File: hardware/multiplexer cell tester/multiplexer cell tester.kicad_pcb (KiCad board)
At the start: 2 copper layers, 143 x 118 mm, 152 parts, among them J1 Conn_01x10_Female, J10 Panel 3, J11 Conn_01x03_Male, J12 Conn_01x03_Male, J13 Conn_01x03_Male, J14 0781710004, J15 Radio, J16 Power, J17 Conn_01x01_Male, J2 Conn_01x10_Female, J3 Conn_01x10_Female, J4 Conn_01x10_Female, J5 A2 Select, J6 A1 Select, J7 A0 Select, J8 Panel 1, J9 Panel 2, U1 SN74LVC1G14DRL, U10 ADG839YKSZ-REEL7, U11 ADG839YKSZ-REEL7, U12 ADG839YKSZ-REEL7, U13 74HC590, U14 ADG841YKSZ-500RL7, U15 ADG841YKSZ-500RL7, U16 ADG841YKSZ-500RL7, U17 ADG841YKSZ-500RL7, U18 ADG841YKSZ-500RL7, U19 ADG841YKSZ-500RL7, U2 SN74LVC1G14DRL, U20 ADG841YKSZ-500RL7, U21 ADG841YKSZ-500RL7, U22 INA190A4IDDFR, U23 OPA2387, U24 INA190A4IDDFR, U25 INA190A4IDDFR, U26 INA190A4IDDFR, U27 LT6654AMPS6-1.25, U28 LT6654AHS6-3.3, U3 CD4518BM96, U4 CD4514BM, U5 ADG839YKSZ-REEL7, U6 ADG839YKSZ-REEL7, U7 ADG839YKSZ-REEL7, U8 ADG839YKSZ-REEL7, U9 ADG839YKSZ-REEL7

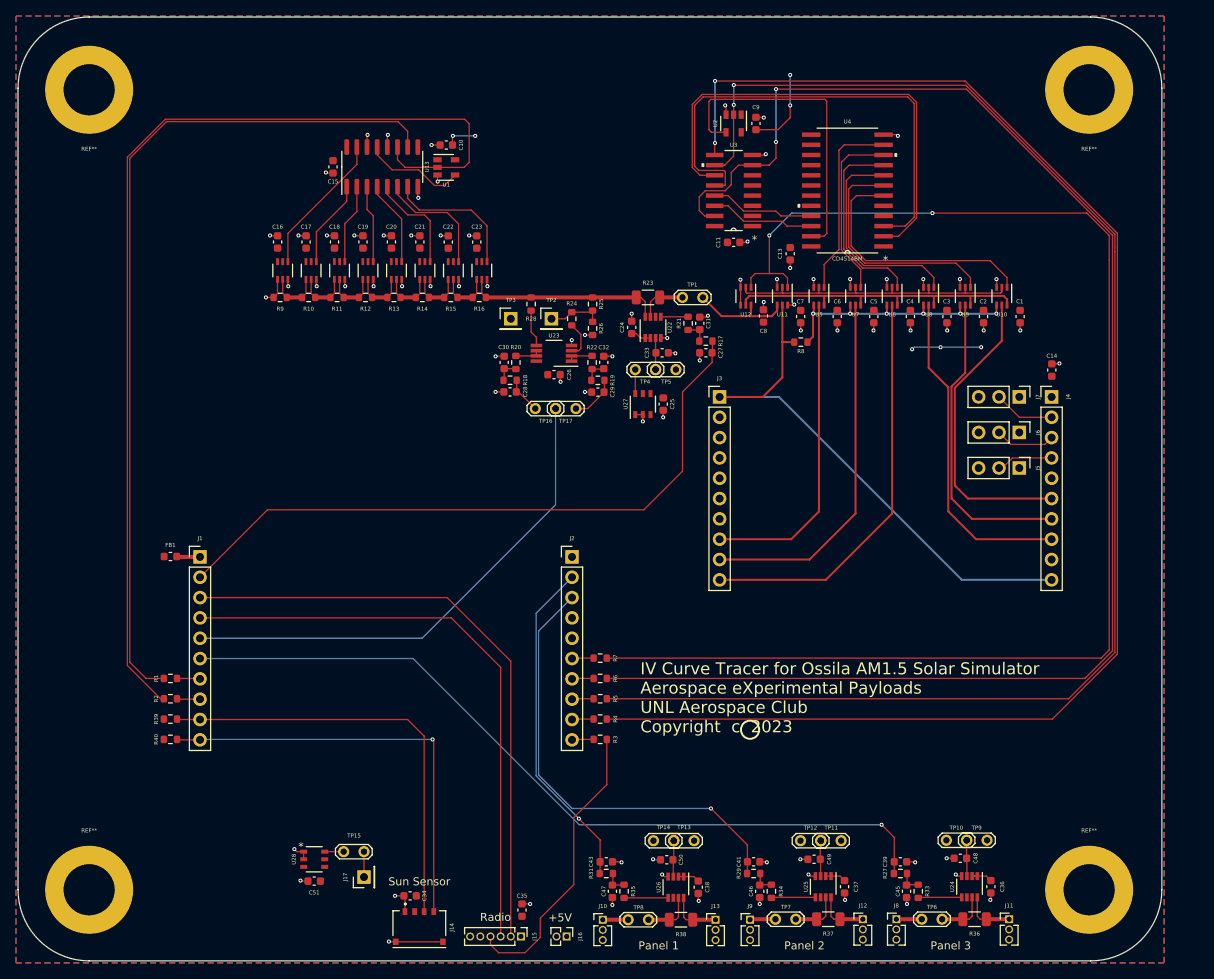
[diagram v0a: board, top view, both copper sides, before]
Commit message: Updating curve tracer
- Remove unused circuits
- Update gerbers and renders
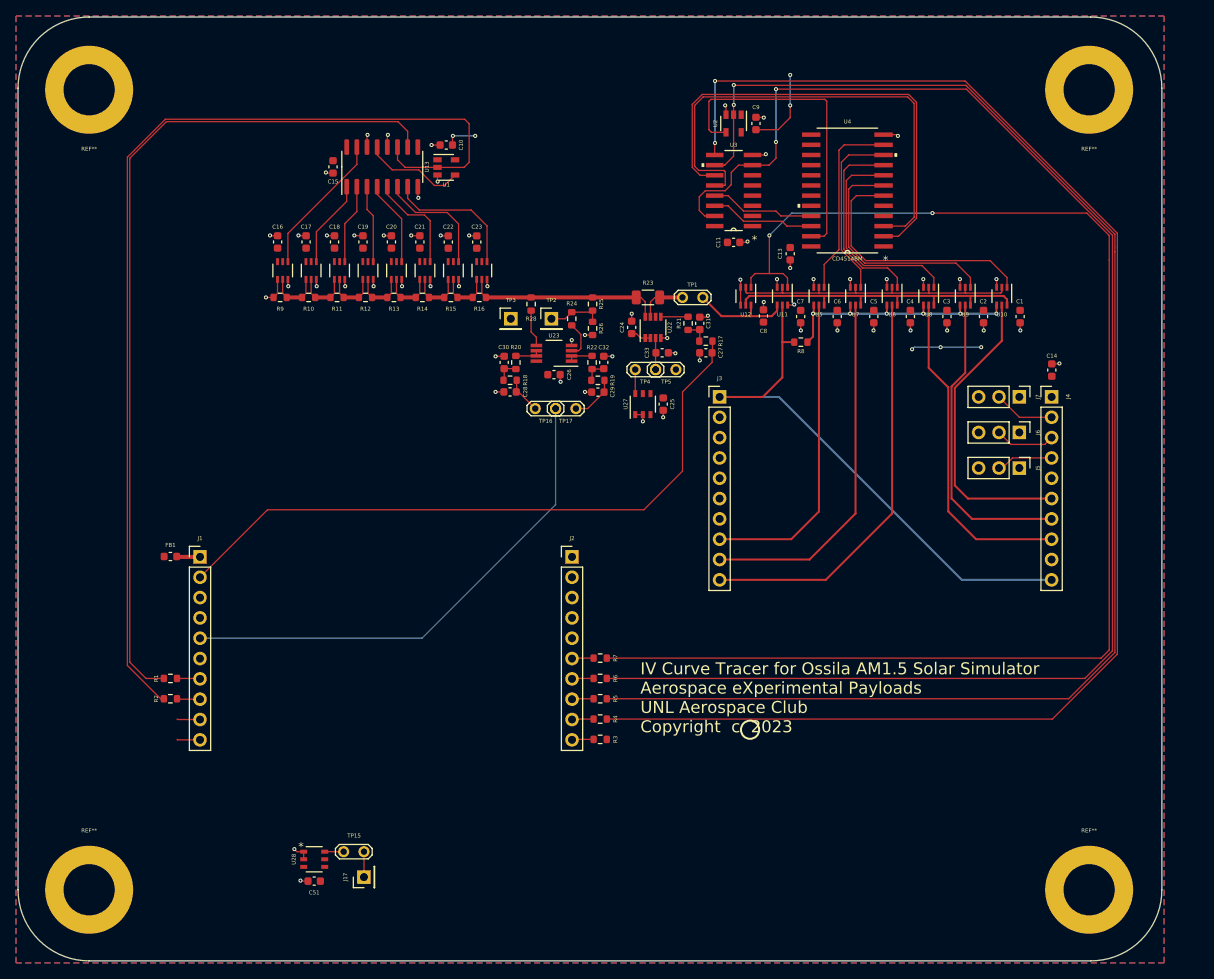
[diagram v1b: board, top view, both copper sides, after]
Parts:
- removed C34, C35, C36, C37, C38, C48, C49, C50: 1u, Capacitor_SMD:C_0603_1608Metric
- removed C39, C41, C43: 10n, Capacitor_SMD:C_0603_1608Metric
- removed C45, C46, C47: 10u, Capacitor_SMD:C_0603_1608Metric
- removed J10: Panel 3, Connector_PinHeader_1.27mm:PinHeader_1x03_P1.27mm_Vertical
- removed J11, J12, J13: Conn_01x03_Male, Connector_PinHeader_1.27mm:PinHeader_1x03_P1.27mm_Vertical
- removed J14: 0781710004, 0781710004:MOLEX_0781710004
- removed J15: Radio, Connector_PinHeader_1.27mm:PinHeader_1x06_P1.27mm_Vertical
- removed J16: Power, Connector_PinHeader_1.27mm:PinHeader_1x02_P1.27mm_Vertical
- removed J8: Panel 1, Connector_PinHeader_1.27mm:PinHeader_1x03_P1.27mm_Vertical
- removed J9: Panel 2, Connector_PinHeader_1.27mm:PinHeader_1x03_P1.27mm_Vertical
- removed R27, R29, R31: 470, Resistor_SMD:R_0603_1608Metric
- removed R33, R34, R35: 10k, Resistor_SMD:R_0603_1608Metric
- removed R36, R37, R38: 510m, Resistor_SMD:R_1206_3216Metric
- removed R39, R40: 4k7, Resistor_SMD:R_0603_1608Metric
- removed TP10, TP11, TP12, TP13, TP14, TP6, TP7, TP8, TP9: Current Test, TestPoint:TestPoint_2Pads_Pitch2.54mm_Drill0.8mm
- removed U24, U25, U26: INA190A4IDDFR, ul_INA190A4IDDFR:INA190A4IDDFR
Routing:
- net PANEL_1: track 100.6 -> 0.00 mm, vias 1 -> 0
- net RX: track 76.6 -> 0.00 mm
- net TX: track 73.8 -> 0.00 mm
- net PANEL_2: track 57.2 -> 0.00 mm, vias 1 -> 0
- net SCL: track 53.7 -> 2.90 mm
- net SDA: track 53.6 -> 2.90 mm, vias 1 -> 0
- net PANEL_3: track 42.2 -> 0.00 mm, vias 1 -> 0
- net BUSY: track 36.7 -> 0.00 mm
- net GND: track 95.7 -> 70.8 mm, vias 81 -> 63
- net +3V3: track 71.7 -> 63.2 mm
- net Net-(J13-Pad1): track 6.54 -> 0.00 mm
- net Net-(J12-Pad1): track 6.50 -> 0.00 mm
- net Net-(J11-Pad1): track 6.50 -> 0.00 mm
- net Net-(R38-Pad2): track 6.30 -> 0.00 mm
- net Net-(R36-Pad2): track 6.26 -> 0.00 mm
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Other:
- board text removed: "+5V"
- board text removed: "Panel 1"
- board text removed: "Panel 2"
- board text removed: "Panel 3"
- board text removed: "Radio"
- board text removed: "Sun Sensor"

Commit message: Create holders
- Created holders for the payload
- Sliced holders for testing
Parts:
- removed C7, C8: 0.1u, Capacitor_SMD:C_0603_1608Metric
- removed U11, U12: ADG839YKSZ-REEL7, ul_ADG839YKSZ-REEL7:ADG839YKSZ-REEL7
- moved R8 7.10 mm to (170.9, 68.2)
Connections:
- J3 pad 1: Net-(J3-Pad1) -> /Curve Tracer/PANEL_VOLTAGE
- J4 pad 10: Net-(J3-Pad1) -> /Curve Tracer/PANEL_VOLTAGE
- R8 pad 1: Net-(J3-Pad1) -> /Curve Tracer/PANEL_VOLTAGE
- U10 pad 6: Net-(U10-Pad6) -> GND
- U5 pad 6: Net-(U10-Pad6) -> GND
- U6 pad 6: Net-(U10-Pad6) -> GND
- U7 pad 6: Net-(U10-Pad6) -> GND
- U8 pad 6: Net-(U10-Pad6) -> GND
- U9 pad 6: Net-(U10-Pad6) -> GND
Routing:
- net REVERSE_BIAS: track 172.0 -> 0.00 mm, vias 2 -> 0
- net Net-(J3-Pad1): track 70.4 -> 0.00 mm
- net /Curve Tracer/PANEL_VOLTAGE: track 12.6 -> 71.8 mm
- net Net-(U10-Pad6): track 40.2 -> 0.00 mm
- net GND: track 70.8 -> 93.3 mm, vias 63 -> 58
- net +3V3: track 63.2 -> 52.7 mm
- net Net-(R8-Pad2): track 33.3 -> 35.4 mm

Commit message: Finalized curve tracer
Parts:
- removed R3, R7: 100, Resistor_SMD:R_0603_1608Metric
- removed U1: SN74LVC1G14DRL, Package_TO_SOT_SMD:SOT-23-5
- added C12: 0.1u, Capacitor_SMD:C_0603_1608Metric, F.Cu at (116.9, 52.3)
- added R27: 400, Resistor_SMD:R_0603_1608Metric, F.Cu at (176.3, 71.9)
- added R29: 400, Resistor_SMD:R_0603_1608Metric, F.Cu at (185.5, 71.9)
- added R30: 400, Resistor_SMD:R_0603_1608Metric, F.Cu at (190.1, 71.9)
- added R31: 400, Resistor_SMD:R_0603_1608Metric, F.Cu at (194.6, 71.9)
- added R32: 400, Resistor_SMD:R_0603_1608Metric, F.Cu at (199.3, 71.9)
- added R33: 100, Resistor_SMD:R_0603_1608Metric, F.Cu at (96.5, 113.3)
- added R34: 4k7, Resistor_SMD:R_0603_1608Metric, F.Cu at (96.5, 121.0)
- added R35: 4k7, Resistor_SMD:R_0603_1608Metric, F.Cu at (96.5, 123.5)
- added U11: CD4516B_PW_16, Package_SO:TSSOP-16_4.4x5mm_P0.65mm, F.Cu at (113.0, 52.3)
- added U12: CD4071BE, Package_SO:TSSOP-14_4.4x5mm_P0.65mm, F.Cu at (123.0, 52.3)
- R8: value 100 -> 400
- U13: value 74HC590 -> CD4516B_PW_16; footprint Package_SO:SOIC-16_3.9x9.9mm_P1.27mm -> Package_SO:TSSOP-16_4.4x5mm_P0.65mm
- moved R8 10.7 mm to (181.0, 71.9), turned to 90 degrees
- moved U13 10.0 mm to (133.0, 52.3), turned to 270 degrees
- moved C10 6.84 mm to (137.1, 52.3), turned to 90 degrees
- moved C15 2.38 mm to (119.2, 52.3)
- moved C4 1.63 mm to (188.0, 71.9)
- moved C5 1.63 mm to (183.4, 71.9)
- moved C3 1.63 mm to (192.6, 71.9)
- moved C6 1.55 mm to (179.0, 71.9)
- moved C1 1.55 mm to (201.8, 71.9)
- moved C2 1.55 mm to (197.3, 71.9)
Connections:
- net PANEL_2 renamed Net-(J2-Pad3)
- net PANEL_3 renamed Net-(J2-Pad2)
- net RX renamed Net-(J1-Pad3)
- net TX renamed Net-(J1-Pad4)
- J1 pad 10: SDA -> /Perovskite Switches/SDA
- J1 pad 6: PANEL_1 -> Net-(J1-Pad6)
- J1 pad 9: SCL -> /Perovskite Switches/SCL
- U10 pad 4: Net-(R8-Pad2) -> Net-(R32-Pad2)
- U13 pad 1: Net-(U13-Pad1) -> GND
- U13 pad 10: ~LADDER_RESET -> LADDER_UD
- U13 pad 11: LADDER_CLOCK -> Net-(U13-Pad11)
- U13 pad 13: /Resistor Ladder/LADDER_LATCH -> GND
- U13 pad 14: GND -> Net-(U13-Pad14)
- U13 pad 15: Net-(U13-Pad15) -> Net-(U12-Pad3)
- U13 pad 3: Net-(U13-Pad3) -> GND
- U13 pad 4: Net-(U13-Pad4) -> GND
- U13 pad 5: Net-(U13-Pad5) -> GND
- U13 pad 9: Net-(U13-Pad9) -> ~LADDER_RESET
- U14 pad 4: Net-(U13-Pad15) -> Net-(U11-Pad6)
- U15 pad 4: Net-(U13-Pad1) -> Net-(U11-Pad11)
- U16 pad 4: Net-(U13-Pad2) -> Net-(U11-Pad14)
- U17 pad 4: Net-(U13-Pad3) -> Net-(U11-Pad2)
- U18 pad 4: Net-(U13-Pad4) -> Net-(U13-Pad6)
- U19 pad 4: Net-(U13-Pad5) -> Net-(U13-Pad11)
- U20 pad 4: Net-(U13-Pad6) -> Net-(U13-Pad14)
- U21 pad 4: Net-(U13-Pad7) -> Net-(U13-Pad2)
- U5 pad 4: Net-(R8-Pad2) -> Net-(R27-Pad2)
- U6 pad 4: Net-(R8-Pad2) -> Net-(R29-Pad2)
- U8 pad 4: Net-(R8-Pad2) -> Net-(R30-Pad2)
- U9 pad 4: Net-(R8-Pad2) -> Net-(R31-Pad2)
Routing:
- net LADDER_UD: track 0.00 -> 105.0 mm, vias 0 -> 3
- net /Perovskite Switches/SDA: track 0.00 -> 86.8 mm
- net /Perovskite Switches/SCL: track 0.00 -> 81.4 mm
- net /Curve Tracer/PANEL_VOLTAGE: track 71.8 -> 114.3 mm, vias 0 -> 7
- net Net-(R8-Pad2): track 35.4 -> 2.09 mm, vias 6 -> 0
- net LADDER_CLOCK: track 130.8 -> 104.0 mm, vias 0 -> 4
- net GND: track 93.3 -> 112.4 mm, vias 58 -> 67
- net Net-(U11-Pad7): track 0.00 -> 18.9 mm
- net Net-(U13-Pad15): track 17.9 -> 0.00 mm
- net Net-(U11-Pad2): track 0.00 -> 17.3 mm
- net Net-(U13-Pad7): track 17.3 -> 0.00 mm
- net Net-(U12-Pad3): track 0.00 -> 16.5 mm, vias 0 -> 2
- net Net-(U11-Pad6): track 0.00 -> 15.7 mm
- net /Resistor Ladder/LADDER_LATCH: track 12.8 -> 0.00 mm
- net Net-(U13-Pad5): track 12.8 -> 0.00 mm
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
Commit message: Final testing
- Finalize hardware, add output capacitor to voltage reference
- Add curve data
- Update curve tracing software to newest hardware
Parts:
- added C7: 1u, Capacitor_SMD:C_0603_1608Metric, F.Cu at (114.6, 135.5)
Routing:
- net Net-(C7-Pad1): track 2.37 -> 4.54 mm
